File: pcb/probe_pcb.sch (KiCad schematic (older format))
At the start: 4 parts

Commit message: Worked on schematic - debug complete.
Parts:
- removed J?: CONN_01X04, symbol CONN_01X04
- removed U?: ST_LINK, symbol ST_LINK
- added D? (x3): LED, symbol LED
- added DS?: LCD-016N002L, WC1602A, symbol LCD-016N002L
- added J? (x2): USB_B, symbol USB_B
- added Q? (x3): PN2222A, TO_SOT_Packages_THT:TO-92_Molded_Narrow, symbol PN2222A
- added R? (x3): 220, symbol R
- added U?: TARGET, STM32F051C6, symbol TARGET
- added U?: ST_LINK, symbol ST_LINK
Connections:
- net labels added: +5V, GND, NRST, SWCLK, SWDIO, USB_B_D+, USB_B_D-, V_Debug, V_Target
- wire segments 0 -> 59
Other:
- note added: "Two of these - one pogo pin one female header."
- note added: "USB 1 - Connects to ST-LINK for flashing target and debugger"
- note added: "USB 2 - For firmware upgrade of DEBUG"
- moved on the sheet: U?

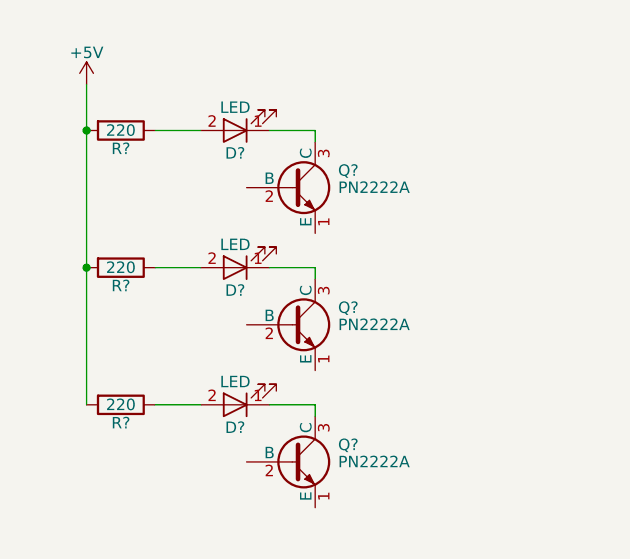
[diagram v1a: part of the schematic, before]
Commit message: Added LEDs
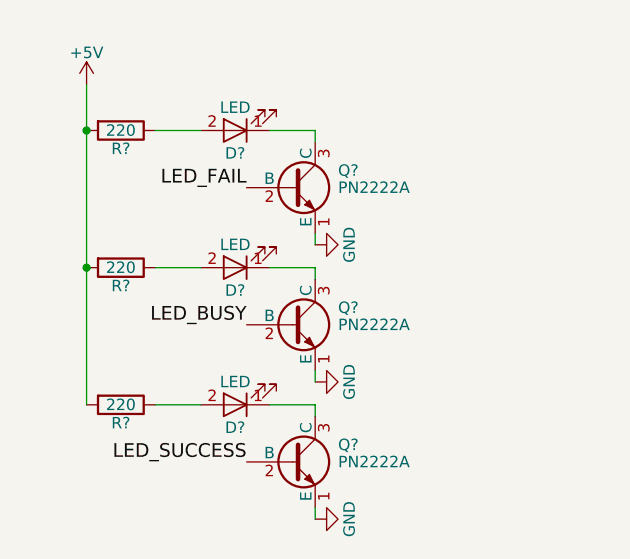
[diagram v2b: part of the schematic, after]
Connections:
- net labels added: LED_BUSY, LED_FAIL, LED_SUCCESS
- wire segments 59 -> 62
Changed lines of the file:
@@
 Wire Wire Line
 	2000 6500 2000 6550
+Text Label 1700 6750 2    60   ~ 0
+LED_BUSY
+Text Label 1700 6150 2    60   ~ 0
+LED_FAIL
+Text Label 1700 7350 2    60   ~ 0
+LED_SUCCESS
+$Comp
+L GND #PWR?
+U 1 1 5975E39F
+P 2000 6400
+F 0 "#PWR?" H 2000 6150 50  0001 C CNN
+F 1 "GND" H 2000 6250 50  0000 C CNN
+F 2 "" H 2000 6400 50  0001 C CNN
+F 3 "" H 2000 6400 50  0001 C CNN
+	1    2000 6400
+	0    -1   -1   0
+$EndComp
+$Comp
+L GND #PWR?
+U 1 1 5975E443
+P 2000 7000
+F 0 "#PWR?" H 2000 6750 50  0001 C CNN
+F 1 "GND" H 2000 6850 50  0000 C CNN
+F 2 "" H 2000 7000 50  0001 C CNN
+F 3 "" H 2000 7000 50  0001 C CNN
+	1    2000 7000
+	0    -1   -1   0
+$EndComp
+$Comp
+L GND #PWR?
+U 1 1 5975E69B
+P 2000 7600
+F 0 "#PWR?" H 2000 7350 50  0001 C CNN
+F 1 "GND" H 2000 7450 50  0000 C CNN
+F 2 "" H 2000 7600 50  0001 C CNN
+F 3 "" H 2000 7600 50  0001 C CNN
+	1    2000 7600
+	0    -1   -1   0
+$EndComp
+Wire Wire Line
+	2000 6350 2000 6400
+Wire Wire Line
+	2000 6950 2000 7000
+Wire Wire Line
+	2000 7550 2000 7600
 $EndSCHEMATC

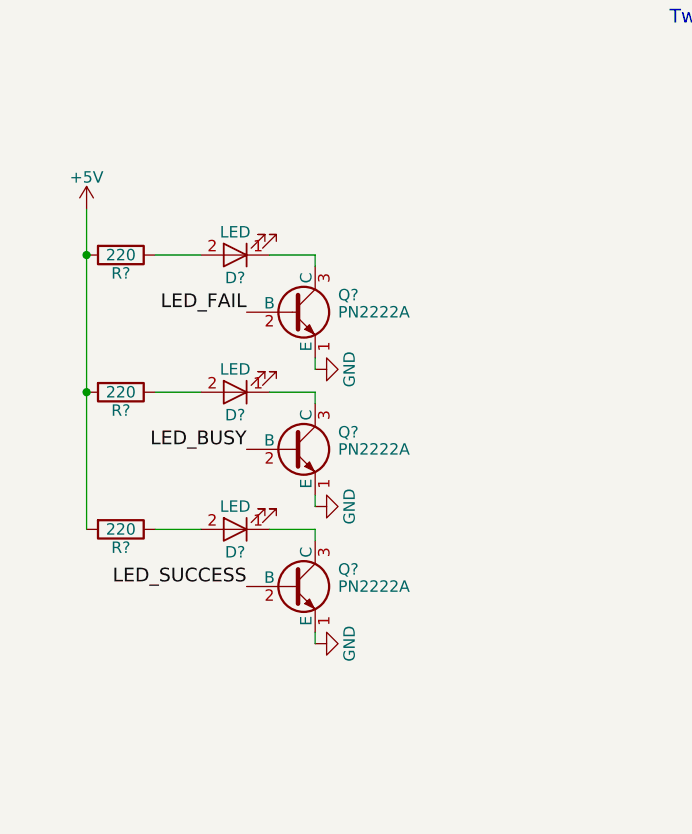
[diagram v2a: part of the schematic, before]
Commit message: Added LEDs (with resistors this time!
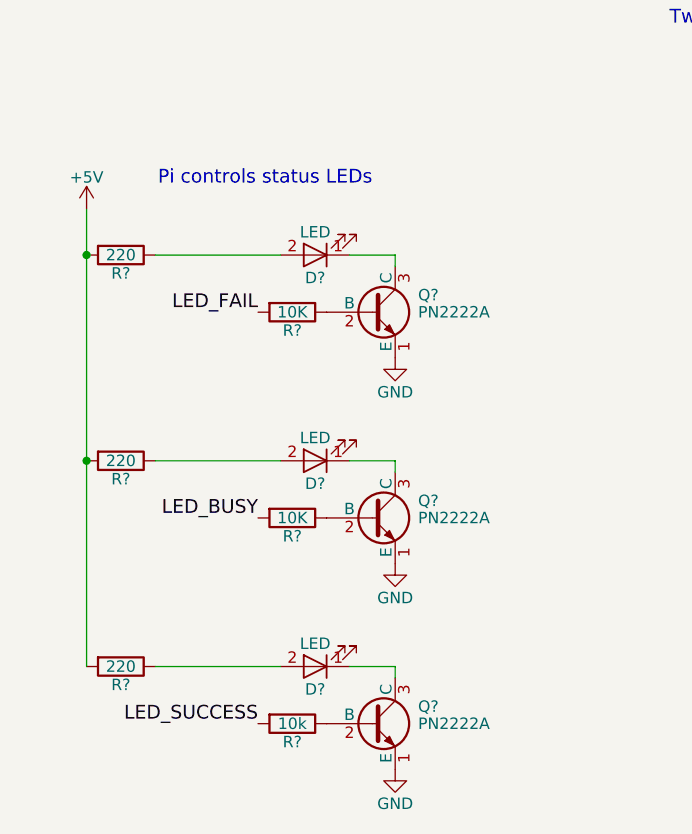
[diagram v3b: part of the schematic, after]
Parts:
- added R? (x2): 10K, symbol R
- added R?: 10k, symbol R
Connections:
- wire segments 62 -> 59
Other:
- note added: "Pi controls status LEDs"
- moved on the sheet: D?, Q?, R?
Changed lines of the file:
@@
 L LED D?
 U 1 1 5975D07A
-P 1650 5900
-F 0 "D?" H 1650 6000 50  0000 C CNN
-F 1 "LED" H 1650 5800 50  0000 C CNN
-F 2 "" H 1650 5900 50  0001 C CNN
-F 3 "" H 1650 5900 50  0001 C CNN
-	1    1650 5900
+P 2000 5900
+F 0 "D?" H 2000 6000 50  0000 C CNN
+F 1 "LED" H 2000 5800 50  0000 C CNN
+F 2 "" H 2000 5900 50  0001 C CNN
+F 3 "" H 2000 5900 50  0001 C CNN
+	1    2000 5900
 	-1   0    0    1
 $EndComp
@@
 L LED D?
 U 1 1 5975D142
-P 1650 6500
-F 0 "D?" H 1650 6600 50  0000 C CNN
-F 1 "LED" H 1650 6400 50  0000 C CNN
-F 2 "" H 1650 6500 50  0001 C CNN
-F 3 "" H 1650 6500 50  0001 C CNN
-	1    1650 6500
+P 2000 6800
+F 0 "D?" H 2000 6900 50  0000 C CNN
+F 1 "LED" H 2000 6700 50  0000 C CNN
+F 2 "" H 2000 6800 50  0001 C CNN
+F 3 "" H 2000 6800 50  0001 C CNN
+	1    2000 6800
 	-1   0    0    1
 $EndComp
@@
 L LED D?
 U 1 1 5975D175
-P 1650 7100
-F 0 "D?" H 1650 7200 50  0000 C CNN
-F 1 "LED" H 1650 7000 50  0000 C CNN
-F 2 "" H 1650 7100 50  0001 C CNN
-F 3 "" H 1650 7100 50  0001 C CNN
-	1    1650 7100
+P 2000 7700
+F 0 "D?" H 2000 7800 50  0000 C CNN
+F 1 "LED" H 2000 7600 50  0000 C CNN
+F 2 "" H 2000 7700 50  0001 C CNN
+F 3 "" H 2000 7700 50  0001 C CNN
+	1    2000 7700
 	-1   0    0    1
 $EndComp
@@
 L R R?
 U 1 1 5975D1B1
-P 1150 6500
-F 0 "R?" V 1230 6500 50  0000 C CNN
-F 1 "220" V 1150 6500 50  0000 C CNN
-F 2 "" V 1080 6500 50  0001 C CNN
-F 3 "" H 1150 6500 50  0001 C CNN
-	1    1150 6500
+P 1150 6800
+F 0 "R?" V 1230 6800 50  0000 C CNN
+F 1 "220" V 1150 6800 50  0000 C CNN
+F 2 "" V 1080 6800 50  0001 C CNN
+F 3 "" H 1150 6800 50  0001 C CNN
+	1    1150 6800
 	0    1    1    0
 $EndComp
@@
 L R R?
 U 1 1 5975D755
-P 1150 7100
-F 0 "R?" V 1230 7100 50  0000 C CNN
-F 1 "220" V 1150 7100 50  0000 C CNN
-F 2 "" V 1080 7100 50  0001 C CNN
-F 3 "" H 1150 7100 50  0001 C CNN
-	1    1150 7100
-	0    1    1    0
-$EndComp
-Wire Wire Line
-	1300 7100 1500 7100
-Wire Wire Line
-	1300 6500 1500 6500
-Wire Wire Line
-	1300 5900 1500 5900
-Wire Wire Line
-	1000 5700 1000 7100
-Connection ~ 1000 6500
+P 1150 7700
+F 0 "R?" V 1230 7700 50  0000 C CNN
+F 1 "220" V 1150 7700 50  0000 C CNN
+F 2 "" V 1080 7700 50  0001 C CNN
+F 3 "" H 1150 7700 50  0001 C CNN
+	1    1150 7700
+	0    1    1    0
+$EndComp
+Wire Wire Line
+	1300 7700 1850 7700
+Wire Wire Line
+	1300 6800 1850 6800
+Wire Wire Line
+	1300 5900 1850 5900
+Wire Wire Line
+	1000 5700 1000 7700
+Connection ~ 1000 6800
 Connection ~ 1000 5900
 $Comp
@@
 L PN2222A Q?
 U 1 1 5975DA2C
-P 1900 6150
-F 0 "Q?" H 2100 6225 50  0000 L CNN
-F 1 "PN2222A" H 2100 6150 50  0000 L CNN
-F 2 "TO_SOT_Packages_THT:TO-92_Molded_Narrow" H 2100 6075 50  0001 L CIN
-F 3 "" H 1900 6150 50  0001 L CNN
-	1    1900 6150
+P 2250 6150
+F 0 "Q?" H 2450 6225 50  0000 L CNN
+F 1 "PN2222A" H 2450 6150 50  0000 L CNN
+F 2 "TO_SOT_Packages_THT:TO-92_Molded_Narrow" H 2450 6075 50  0001 L CIN
+F 3 "" H 2250 6150 50  0001 L CNN
+	1    2250 6150
 	1    0    0    -1
 $EndComp
@@
 L PN2222A Q?
 U 1 1 5975DAA9
-P 1900 7350
-F 0 "Q?" H 2100 7425 50  0000 L CNN
-F 1 "PN2222A" H 2100 7350 50  0000 L CNN
-F 2 "TO_SOT_Packages_THT:TO-92_Molded_Narrow" H 2100 7275 50  0001 L CIN
-F 3 "" H 1900 7350 50  0001 L CNN
-	1    1900 7350
+P 2250 7950
+F 0 "Q?" H 2450 8025 50  0000 L CNN
+F 1 "PN2222A" H 2450 7950 50  0000 L CNN
+F 2 "TO_SOT_Packages_THT:TO-92_Molded_Narrow" H 2450 7875 50  0001 L CIN
+F 3 "" H 2250 7950 50  0001 L CNN
+	1    2250 7950
 	1    0    0    -1
 $EndComp
@@
 L PN2222A Q?
 U 1 1 5975DD76
-P 1900 6750
-F 0 "Q?" H 2100 6825 50  0000 L CNN
-F 1 "PN2222A" H 2100 6750 50  0000 L CNN
-F 2 "TO_SOT_Packages_THT:TO-92_Molded_Narrow" H 2100 6675 50  0001 L CIN
-F 3 "" H 1900 6750 50  0001 L CNN
-	1    1900 6750
-	1    0    0    -1
-$EndComp
-Wire Wire Line
-	1800 5900 2000 5900
-Wire Wire Line
-	2000 5900 2000 5950
-Wire Wire Line
-	1800 6500 2000 6500
-Wire Wire Line
-	1800 7100 2000 7100
-Wire Wire Line
-	2000 7100 2000 7150
-Wire Wire Line
-	2000 6500 2000 6550
-Text Label 1700 6750 2    60   ~ 0
+P 2250 7050
+F 0 "Q?" H 2450 7125 50  0000 L CNN
+F 1 "PN2222A" H 2450 7050 50  0000 L CNN
+F 2 "TO_SOT_Packages_THT:TO-92_Molded_Narrow" H 2450 6975 50  0001 L CIN
+F 3 "" H 2250 7050 50  0001 L CNN
+	1    2250 7050
+	1    0    0    -1
+$EndComp
+Wire Wire Line
+	2150 5900 2350 5900
+Wire Wire Line
+	2350 5900 2350 5950
+Wire Wire Line
+	2150 6800 2350 6800
+Wire Wire Line
+	2150 7700 2350 7700
+Wire Wire Line
+	2350 7700 2350 7750
+Wire Wire Line
+	2350 6800 2350 6850
+Text Label 1750 7050 2    60   ~ 0
 LED_BUSY
-Text Label 1700 6150 2    60   ~ 0
+Text Label 1750 6150 2    60   ~ 0
 LED_FAIL
-Text Label 1700 7350 2    60   ~ 0
+Text Label 1750 7950 2    60   ~ 0
 LED_SUCCESS
 $Comp
 L GND #PWR?
 U 1 1 5975E39F
-P 2000 6400
-F 0 "#PWR?" H 2000 6150 50  0001 C CNN
-F 1 "GND" H 2000 6250 50  0000 C CNN
-F 2 "" H 2000 6400 50  0001 C CNN
-F 3 "" H 2000 6400 50  0001 C CNN
-	1    2000 6400
-	0    -1   -1   0
+P 2350 6350
+F 0 "#PWR?" H 2350 6100 50  0001 C CNN
+F 1 "GND" H 2350 6200 50  0000 C CNN
+F 2 "" H 2350 6350 50  0001 C CNN
+F 3 "" H 2350 6350 50  0001 C CNN
+	1    2350 6350
+	1    0    0    -1
 $EndComp
 $Comp
 L GND #PWR?
 U 1 1 5975E443
-P 2000 7000
-F 0 "#PWR?" H 2000 6750 50  0001 C CNN
-F 1 "GND" H 2000 6850 50  0000 C CNN
-F 2 "" H 2000 7000 50  0001 C CNN
-F 3 "" H 2000 7000 50  0001 C CNN
-	1    2000 7000
-	0    -1   -1   0
+P 2350 7250
+F 0 "#PWR?" H 2350 7000 50  0001 C CNN
+F 1 "GND" H 2350 7100 50  0000 C CNN
+F 2 "" H 2350 7250 50  0001 C CNN
+F 3 "" H 2350 7250 50  0001 C CNN
+	1    2350 7250
+	1    0    0    -1
 $EndComp
 $Comp
 L GND #PWR?
 U 1 1 5975E69B
-P 2000 7600
-F 0 "#PWR?" H 2000 7350 50  0001 C CNN
-F 1 "GND" H 2000 7450 50  0000 C CNN
-F 2 "" H 2000 7600 50  0001 C CNN
-F 3 "" H 2000 7600 50  0001 C CNN
-	1    2000 7600
-	0    -1   -1   0
-$EndComp
-Wire Wire Line
-	2000 6350 2000 6400
-Wire Wire Line
-	2000 6950 2000 7000
-Wire Wire Line
-	2000 7550 2000 7600
+P 2350 8150
+F 0 "#PWR?" H 2350 7900 50  0001 C CNN
+F 1 "GND" H 2350 8000 50  0000 C CNN
+F 2 "" H 2350 8150 50  0001 C CNN
+F 3 "" H 2350 8150 50  0001 C CNN
+	1    2350 8150
+	1    0    0    -1
+$EndComp
+$Comp
+L R R?
+U 1 1 5975F7CC
+P 1900 6150
+F 0 "R?" V 1980 6150 50  0000 C CNN
+F 1 "10K" V 1900 6150 50  0000 C CNN
+F 2 "" V 1830 6150 50  0001 C CNN
+F 3 "" H 1900 6150 50  0001 C CNN
+	1    1900 6150
+	0    1    1    0
+$EndComp
+$Comp
+L R R?
+U 1 1 5975F87C
+P 1900 7050
+F 0 "R?" V 1980 7050 50  0000 C CNN
+F 1 "10K" V 1900 7050 50  0000 C CNN
+F 2 "" V 1830 7050 50  0001 C CNN
+F 3 "" H 1900 7050 50  0001 C CNN
+	1    1900 7050
+	0    1    1    0
+$EndComp
+$Comp
+L R R?
+U 1 1 5975F8F1
+P 1900 7950
+F 0 "R?" V 1980 7950 50  0000 C CNN
+F 1 "10k" V 1900 7950 50  0000 C CNN
+F 2 "" V 1830 7950 50  0001 C CNN
+F 3 "" H 1900 7950 50  0001 C CNN
+	1    1900 7950
+	0    1    1    0
+$EndComp
+Text Notes 2250 5600 2    60   ~ 0
+Pi controls status LEDs
 $EndSCHEMATC
